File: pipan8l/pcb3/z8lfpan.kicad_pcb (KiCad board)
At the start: 2 copper layers, 262.3 x 76.2 mm, 64 parts, among them J1 2x18edgecon, J2 2x18edgecon, J3 2x18edgecon, J4 2x18edgecon, J5 Conn_02x20_Odd_Even, J6 Conn_01x02_Pin, J7 Conn_01x16, J8 Conn_01x12, Q1 2N3906, Q10 2N3906, Q11 2N3906, Q12 2N3906, Q13 2N3906, Q14 2N3906, Q15 2N3906, Q16 2N3906, Q17 2N7000, Q18 2N7000, Q2 2N3906, Q3 2N3906, Q4 2N3906, Q5 2N3906, Q6 2N3906, Q7 2N3906, Q8 2N3906, Q9 2N3906, U1 MCP23017, U2 MCP23017, U3 MCP23017, U4 MCP23017

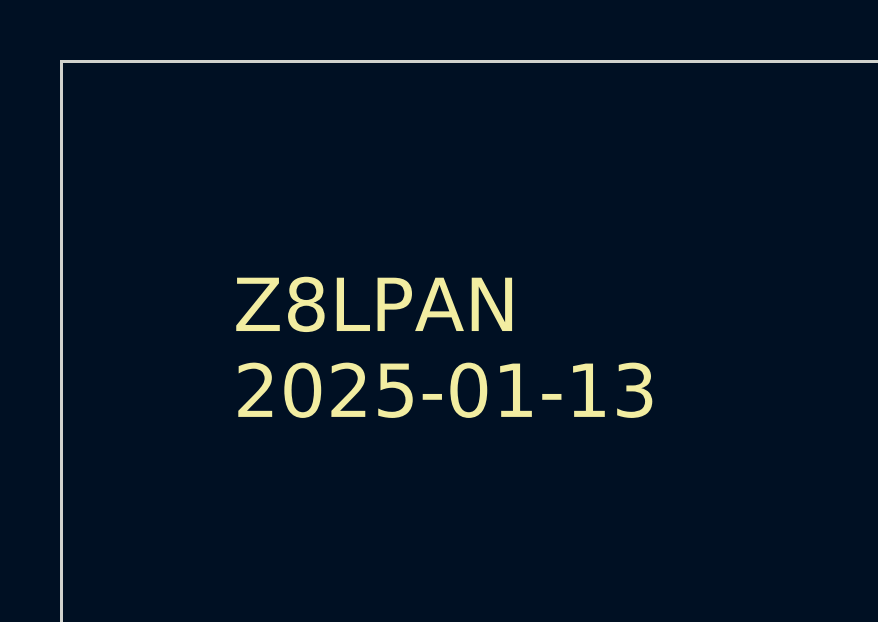
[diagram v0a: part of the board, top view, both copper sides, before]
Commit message: rename pipan8l pcb3 to z8lfpan - it is for use with zynq stuff
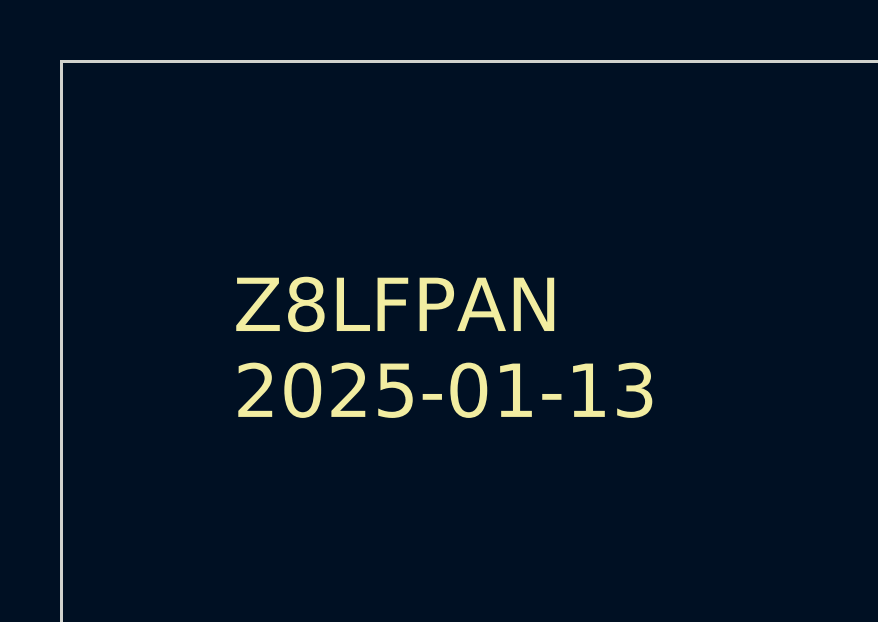
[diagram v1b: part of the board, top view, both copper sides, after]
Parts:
- J1: footprint mypipan8lfoots:backpins-A -> myz8lfpanfoots:backpins-A
- J2: footprint mypipan8lfoots:backpins-B -> myz8lfpanfoots:backpins-B
- J3: footprint mypipan8lfoots:backpins-C -> myz8lfpanfoots:backpins-C
- J4: footprint mypipan8lfoots:backpins-D -> myz8lfpanfoots:backpins-D
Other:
- board text added: "Z8LFPAN 2025-01-13"
- board text removed: "Z8LPAN 2025-01-13"
